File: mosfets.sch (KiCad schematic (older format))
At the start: 28 parts, among them Q11 PSMN1R2-30YLC,115, Q12 PSMN1R2-30YLC,115, Q13 PSMN1R2-30YLC,115, Q14 PMPB20EN, Q15 PMPB20EN, Q16 PMPB20EN, Q17 PMPB20EN

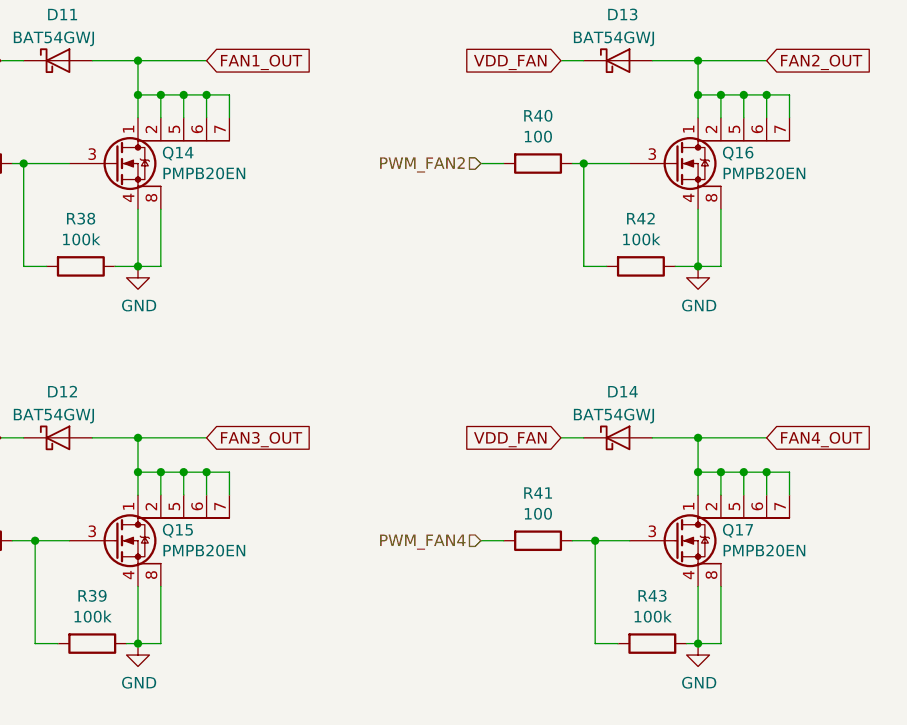
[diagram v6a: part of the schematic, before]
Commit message: Fix MOSFET selection
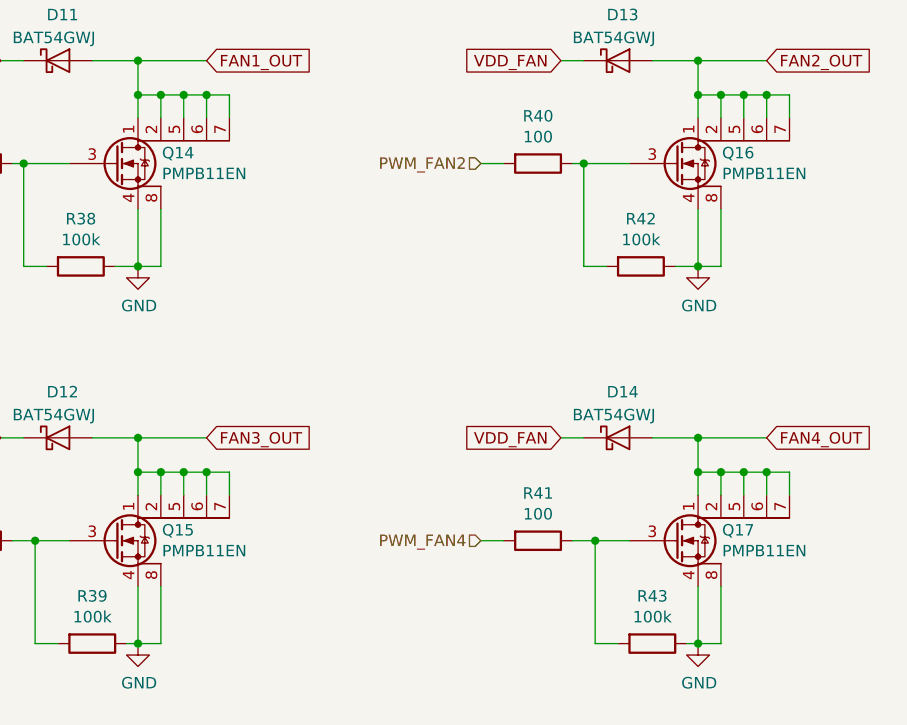
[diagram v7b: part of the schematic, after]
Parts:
- Q14, Q15, Q16, Q17: value PMPB20EN -> PMPB11EN
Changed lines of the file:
@@
 P 5750 1750
 F 0 "Q14" H 5955 1796 50  0000 L CNN
-F 1 "PMPB20EN" H 5955 1705 50  0000 L CNN
+F 1 "PMPB11EN" H 5955 1705 50  0000 L CNN
 F 2 "heteromycin:SOT1220" H 5950 1675 50  0001 L CIN
-F 3 "https://assets.nexperia.com/documents/data-sheet/PMPB20EN.pdf" H 5750 1750 50  0001 L CNN
+F 3 "https://assets.nexperia.com/documents/data-sheet/PMPB11EN.pdf" H 5750 1750 50  0001 L CNN
 	1    5750 1750
 	1    0    0    -1
@@
 P 5750 3400
 F 0 "Q15" H 5955 3446 50  0000 L CNN
-F 1 "PMPB20EN" H 5955 3355 50  0000 L CNN
+F 1 "PMPB11EN" H 5955 3355 50  0000 L CNN
 F 2 "heteromycin:SOT1220" H 5950 3325 50  0001 L CIN
-F 3 "https://assets.nexperia.com/documents/data-sheet/PMPB20EN.pdf" H 5750 3400 50  0001 L CNN
+F 3 "https://assets.nexperia.com/documents/data-sheet/PMPB11EN.pdf" H 5750 3400 50  0001 L CNN
 	1    5750 3400
 	1    0    0    -1
@@
 P 8200 1750
 F 0 "Q16" H 8405 1796 50  0000 L CNN
-F 1 "PMPB20EN" H 8405 1705 50  0000 L CNN
+F 1 "PMPB11EN" H 8405 1705 50  0000 L CNN
 F 2 "heteromycin:SOT1220" H 8400 1675 50  0001 L CIN
-F 3 "https://assets.nexperia.com/documents/data-sheet/PMPB20EN.pdf" H 8200 1750 50  0001 L CNN
+F 3 "https://assets.nexperia.com/documents/data-sheet/PMPB11EN.pdf" H 8200 1750 50  0001 L CNN
 	1    8200 1750
 	1    0    0    -1
@@
 P 8200 3400
 F 0 "Q17" H 8405 3446 50  0000 L CNN
-F 1 "PMPB20EN" H 8405 3355 50  0000 L CNN
+F 1 "PMPB11EN" H 8405 3355 50  0000 L CNN
 F 2 "heteromycin:SOT1220" H 8400 3325 50  0001 L CIN
-F 3 "https://assets.nexperia.com/documents/data-sheet/PMPB20EN.pdf" H 8200 3400 50  0001 L CNN
+F 3 "https://assets.nexperia.com/documents/data-sheet/PMPB11EN.pdf" H 8200 3400 50  0001 L CNN
 	1    8200 3400
 	1    0    0    -1

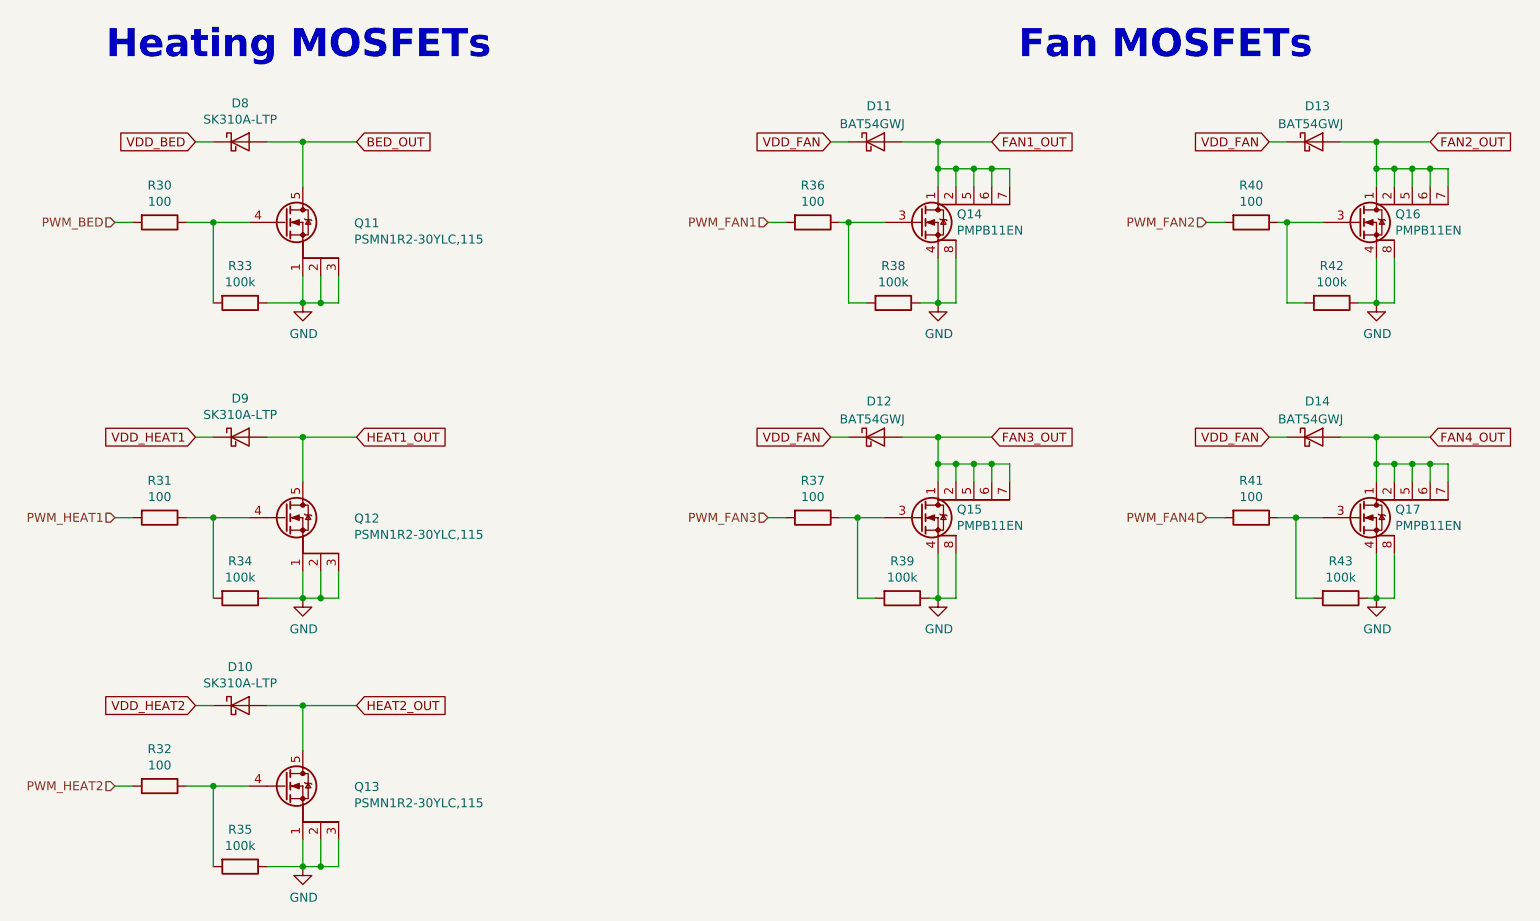
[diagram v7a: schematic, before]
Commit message: Add transistor for boot selection
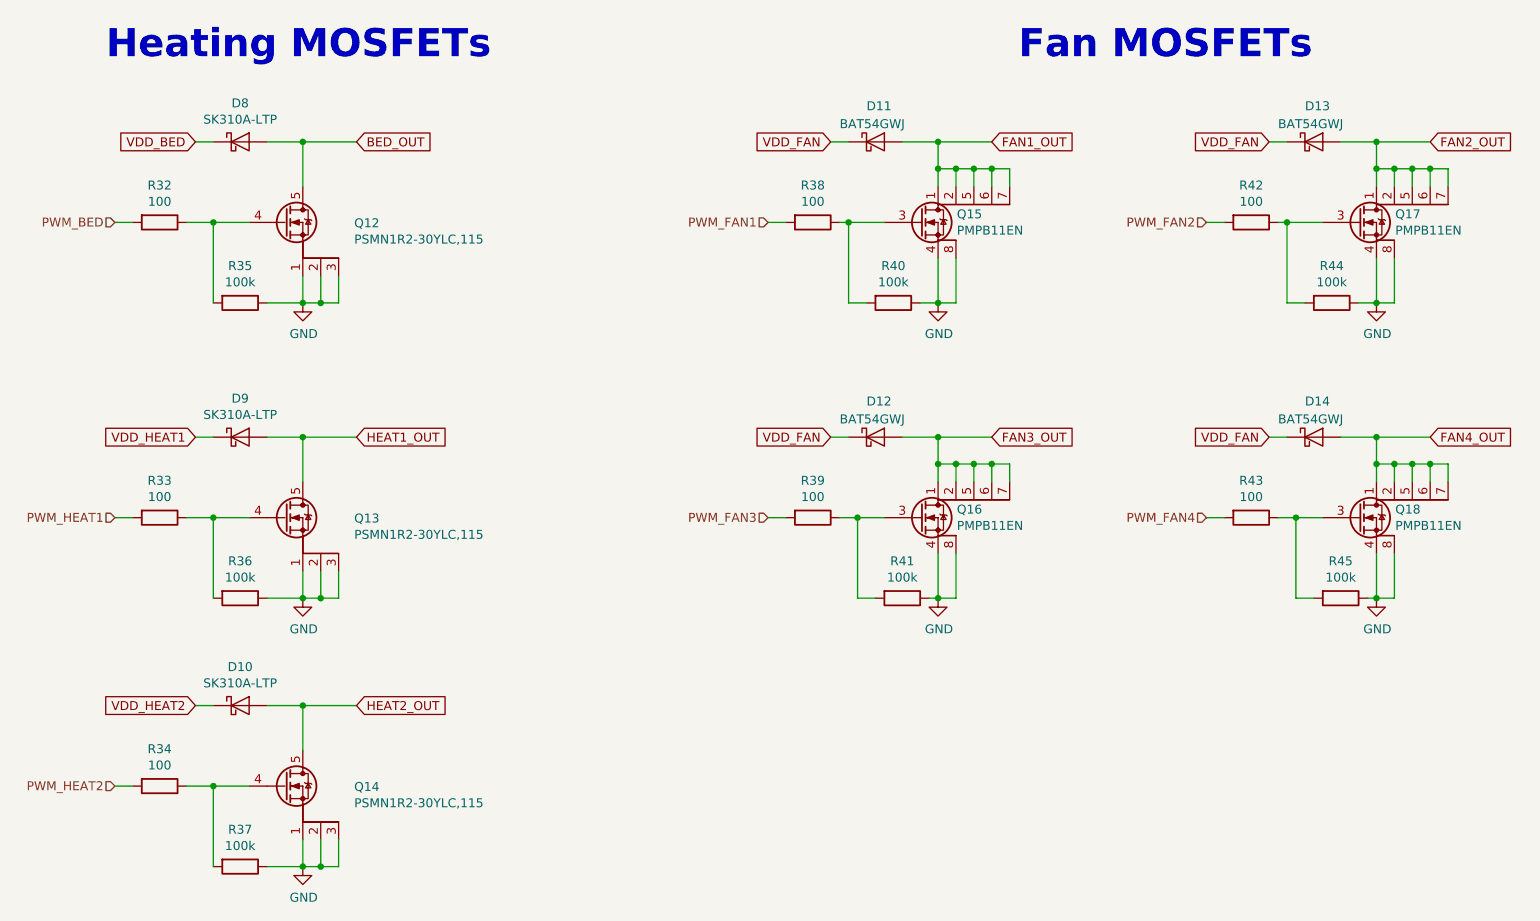
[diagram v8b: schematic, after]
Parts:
- renumbered Q11 to Q12, Q12 to Q13, Q13 to Q14, Q14 to Q15, Q15 to Q16, Q16 to Q17, Q17 to Q18, R30 to R32, R31 to R33, R32 to R34, R33 to R35, R34 to R36, R35 to R37, R36 to R38, R37 to R39, R38 to R40, R39 to R41, R40 to R42, R41 to R43, R42 to R44, R43 to R45
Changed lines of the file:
@@
 	1700 1300 1800 1300
 $Comp
-L heteromycin:PSMN1R8-40YLC,115 Q11
+L heteromycin:PSMN1R8-40YLC,115 Q12
 U 1 1 5B1A764D
 P 2200 1750
-F 0 "Q11" H 2587 1746 50  0000 L CNN
+F 0 "Q12" H 2587 1746 50  0000 L CNN
 F 1 "PSMN1R2-30YLC,115" H 2587 1655 50  0000 L CNN
 F 2 "heteromycin:SOT-669_LFPAK_ThermalVias-1" H 2400 1675 50  0001 L CIN
@@
 PWM_HEAT1
 $Comp
-L Device:R R30
+L Device:R R32
 U 1 1 5B1AEA5D
 P 1500 1750
-F 0 "R30" V 1293 1750 50  0000 C CNN
+F 0 "R32" V 1293 1750 50  0000 C CNN
 F 1 "100" V 1384 1750 50  0000 C CNN
 F 2 "Resistor_SMD:R_0603_1608Metric" V 1430 1750 50  0001 C CNN
@@
 	2300 3850 2300 3700
 $Comp
-L Device:R R31
+L Device:R R33
 U 1 1 5B1B03DE
 P 1500 3400
-F 0 "R31" V 1293 3400 50  0000 C CNN
+F 0 "R33" V 1293 3400 50  0000 C CNN
 F 1 "100" V 1384 3400 50  0000 C CNN
 F 2 "Resistor_SMD:R_0603_1608Metric" V 1430 3400 50  0001 C CNN
@@
 Connection ~ 2300 2950
 $Comp
-L heteromycin:PMPB20EN Q14
+L heteromycin:PMPB20EN Q15
 U 1 1 5B1FB146
 P 5750 1750
-F 0 "Q14" H 5955 1796 50  0000 L CNN
+F 0 "Q15" H 5955 1796 50  0000 L CNN
 F 1 "PMPB11EN" H 5955 1705 50  0000 L CNN
 F 2 "heteromycin:SOT1220" H 5950 1675 50  0001 L CIN
@@
 $EndComp
 $Comp
-L Device:R R36
+L Device:R R38
 U 1 1 5B1FB287
 P 5150 1750
-F 0 "R36" V 4943 1750 50  0000 C CNN
+F 0 "R38" V 4943 1750 50  0000 C CNN
 F 1 "100" V 5034 1750 50  0000 C CNN
 F 2 "Resistor_SMD:R_0603_1608Metric" V 5080 1750 50  0001 C CNN
@@
 	5850 1950 5850 2200
 $Comp
-L Device:R R37
+L Device:R R39
 U 1 1 5B2008D0
 P 5150 3400
-F 0 "R37" V 4943 3400 50  0000 C CNN
+F 0 "R39" V 4943 3400 50  0000 C CNN
 F 1 "100" V 5034 3400 50  0000 C CNN
 F 2 "Resistor_SMD:R_0603_1608Metric" V 5080 3400 50  0001 C CNN
@@
 	1650 3400 1800 3400
 $Comp
-L Device:R R33
+L Device:R R35
 U 1 1 5AF82135
 P 1950 2200
-F 0 "R33" V 1743 2200 50  0000 C CNN
+F 0 "R35" V 1743 2200 50  0000 C CNN
 F 1 "100k" V 1834 2200 50  0000 C CNN
 F 2 "Resistor_SMD:R_0603_1608Metric" V 1880 2200 50  0001 C CNN
@@
 	1800 1750 2000 1750
 $Comp
-L Device:R R34
+L Device:R R36
 U 1 1 5AF8339E
 P 1950 3850
-F 0 "R34" V 1743 3850 50  0000 C CNN
+F 0 "R36" V 1743 3850 50  0000 C CNN
 F 1 "100k" V 1834 3850 50  0000 C CNN
 F 2 "Resistor_SMD:R_0603_1608Metric" V 1880 3850 50  0001 C CNN
@@
 	2300 3850 2100 3850
 $Comp
-L Device:R R38
+L Device:R R40
 U 1 1 5AF83BB4
 P 5600 2200
-F 0 "R38" V 5393 2200 50  0000 C CNN
+F 0 "R40" V 5393 2200 50  0000 C CNN
 F 1 "100k" V 5484 2200 50  0000 C CNN
 F 2 "Resistor_SMD:R_0603_1608Metric" V 5530 2200 50  0001 C CNN
@@
 Connection ~ 5350 1750
 $Comp
-L Device:R R39
+L Device:R R41
 U 1 1 5AF880C0
 P 5650 3850
-F 0 "R39" V 5443 3850 50  0000 C CNN
+F 0 "R41" V 5443 3850 50  0000 C CNN
 F 1 "100k" V 5534 3850 50  0000 C CNN
 F 2 "Resistor_SMD:R_0603_1608Metric" V 5580 3850 50  0001 C CNN
@@
 VDD_FAN
 $Comp
-L heteromycin:PSMN1R8-40YLC,115 Q12
+L heteromycin:PSMN1R8-40YLC,115 Q13
 U 1 1 5BC30682
 P 2200 3400
-F 0 "Q12" H 2587 3396 50  0000 L CNN
+F 0 "Q13" H 2587 3396 50  0000 L CNN
 F 1 "PSMN1R2-30YLC,115" H 2587 3305 50  0000 L CNN
 F 2 "heteromycin:SOT-669_LFPAK_ThermalVias-1" H 2400 3325 50  0001 L CIN
@@
 $EndComp
 $Comp
-L heteromycin:PMPB20EN Q15
+L heteromycin:PMPB20EN Q16
 U 1 1 5BC35639
 P 5750 3400
-F 0 "Q15" H 5955 3446 50  0000 L CNN
+F 0 "Q16" H 5955 3446 50  0000 L CNN
 F 1 "PMPB11EN" H 5955 3355 50  0000 L CNN
 F 2 "heteromycin:SOT1220" H 5950 3325 50  0001 L CIN
@@
 	2300 5350 2300 5200
 $Comp
-L Device:R R32
+L Device:R R34
 U 1 1 5BC4CDF3
 P 1500 4900
-F 0 "R32" V 1293 4900 50  0000 C CNN
+F 0 "R34" V 1293 4900 50  0000 C CNN
 F 1 "100" V 1384 4900 50  0000 C CNN
 F 2 "Resistor_SMD:R_0603_1608Metric" V 1430 4900 50  0001 C CNN
@@
 	1650 4900 1800 4900
 $Comp
-L Device:R R35
+L Device:R R37
 U 1 1 5BC4CE00
 P 1950 5350
-F 0 "R35" V 1743 5350 50  0000 C CNN
+F 0 "R37" V 1743 5350 50  0000 C CNN
 F 1 "100k" V 1834 5350 50  0000 C CNN
 F 2 "Resistor_SMD:R_0603_1608Metric" V 1880 5350 50  0001 C CNN
@@
 	1800 4900 2000 4900
 $Comp
-L heteromycin:PSMN1R8-40YLC,115 Q13
+L heteromycin:PSMN1R8-40YLC,115 Q14
 U 1 1 5BC4CE0B
 P 2200 4900
-F 0 "Q13" H 2587 4896 50  0000 L CNN
+F 0 "Q14" H 2587 4896 50  0000 L CNN
 F 1 "PSMN1R2-30YLC,115" H 2587 4805 50  0000 L CNN
 F 2 "heteromycin:SOT-669_LFPAK_ThermalVias-1" H 2400 4825 50  0001 L CIN
@@
 $EndComp
 $Comp
-L heteromycin:PMPB20EN Q16
+L heteromycin:PMPB20EN Q17
 U 1 1 5BC57CCA
 P 8200 1750
-F 0 "Q16" H 8405 1796 50  0000 L CNN
+F 0 "Q17" H 8405 1796 50  0000 L CNN
 F 1 "PMPB11EN" H 8405 1705 50  0000 L CNN
 F 2 "heteromycin:SOT1220" H 8400 1675 50  0001 L CIN
@@
 $EndComp
 $Comp
-L Device:R R40
+L Device:R R42
 U 1 1 5BC57CD1
 P 7600 1750
-F 0 "R40" V 7393 1750 50  0000 C CNN
+F 0 "R42" V 7393 1750 50  0000 C CNN
 F 1 "100" V 7484 1750 50  0000 C CNN
 F 2 "Resistor_SMD:R_0603_1608Metric" V 7530 1750 50  0001 C CNN
@@
 	8300 1950 8300 2200
 $Comp
-L Device:R R41
+L Device:R R43
 U 1 1 5BC57CE1
 P 7600 3400
-F 0 "R41" V 7393 3400 50  0000 C CNN
+F 0 "R43" V 7393 3400 50  0000 C CNN
 F 1 "100" V 7484 3400 50  0000 C CNN
 F 2 "Resistor_SMD:R_0603_1608Metric" V 7530 3400 50  0001 C CNN
@@
 	7800 1750 8000 1750
 $Comp
-L Device:R R42
+L Device:R R44
 U 1 1 5BC57CF2
 P 8050 2200
-F 0 "R42" V 7843 2200 50  0000 C CNN
+F 0 "R44" V 7843 2200 50  0000 C CNN
 F 1 "100k" V 7934 2200 50  0000 C CNN
 F 2 "Resistor_SMD:R_0603_1608Metric" V 7980 2200 50  0001 C CNN
@@
 Connection ~ 7800 1750
 $Comp
-L Device:R R43
+L Device:R R45
 U 1 1 5BC57CFF
 P 8100 3850
-F 0 "R43" V 7893 3850 50  0000 C CNN
+F 0 "R45" V 7893 3850 50  0000 C CNN
 F 1 "100k" V 7984 3850 50  0000 C CNN
 F 2 "Resistor_SMD:R_0603_1608Metric" V 8030 3850 50  0001 C CNN
@@
 $EndComp
 $Comp
-L heteromycin:PMPB20EN Q17
+L heteromycin:PMPB20EN Q18
 U 1 1 5BC57D1D
 P 8200 3400
-F 0 "Q17" H 8405 3446 50  0000 L CNN
+F 0 "Q18" H 8405 3446 50  0000 L CNN
 F 1 "PMPB11EN" H 8405 3355 50  0000 L CNN
 F 2 "heteromycin:SOT1220" H 8400 3325 50  0001 L CIN
